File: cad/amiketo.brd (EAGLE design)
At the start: 64 x 35 mm, 58 parts, among them CN1 MICROSDPLAIN, J1 HEADER-5X1, Q1 IRLML6344TRPBF, Q2 DMP2035U-7, SW2 SWITCHKMR211, SW3 SWITCHKMR211, U1 STM32F411/48, U2 LSM303D, U3 ADP5062, U4 MCP1824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

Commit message: lis3dh accel
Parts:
- removed C12: 4.7u, jaw:SMD0603
- removed C13: .22u, jaw:SMD0603
- U2: value LSM303D -> LIS3DH
- moved C14 8.00 mm to (34.5, 31.0)
- moved U2 1.12 mm to (38.0, 31.0)
- moved D1 0.54 mm to (32.5, 31.0)
- moved NOISY1 0.50 mm to (27.7, 31.3)
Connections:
- removed net N$1: C12.1, U2.15
- removed net N$2: C13.2, U2.3
- removed net N$4: C13.1, U2.2
- net GND: no longer C12.2, U2.13, U2.16
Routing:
- net N$4: track 7.66 -> 0.00 mm
- net N$2: track 5.94 -> 0.00 mm
- net GND: track 146.6 -> 141.6 mm, vias 79 -> 80
- net IMUINT: track 22.5 -> 18.7 mm
- net I2CCL: track 111.4 -> 108.8 mm, vias 3 -> 4
- net VCC: track 67.7 -> 70.1 mm, vias 15 -> 13
- net N$1: track 2.31 -> 0.00 mm
- net I2CDA: track 110.5 -> 109.9 mm, vias 5 -> 4
- net N$14: track 11.5 -> 10.9 mm

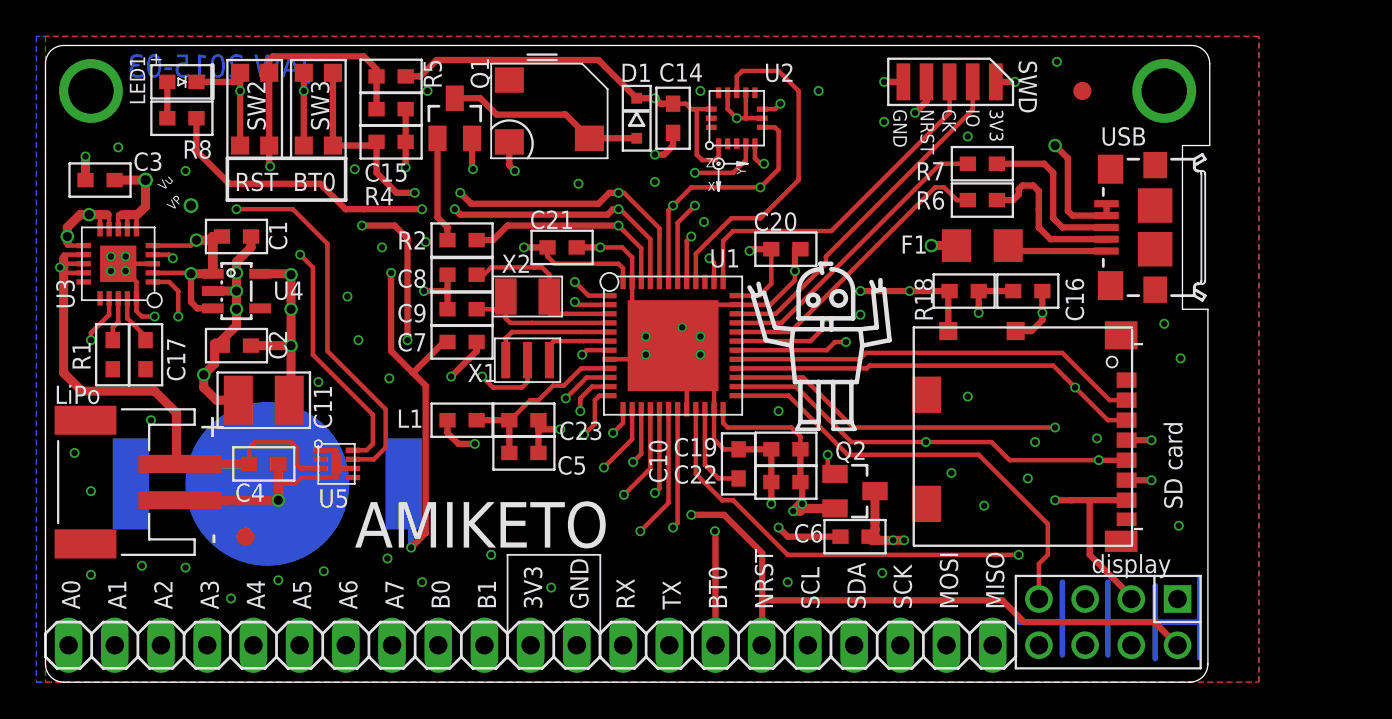
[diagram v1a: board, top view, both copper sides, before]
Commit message: move usb, embiggen sd
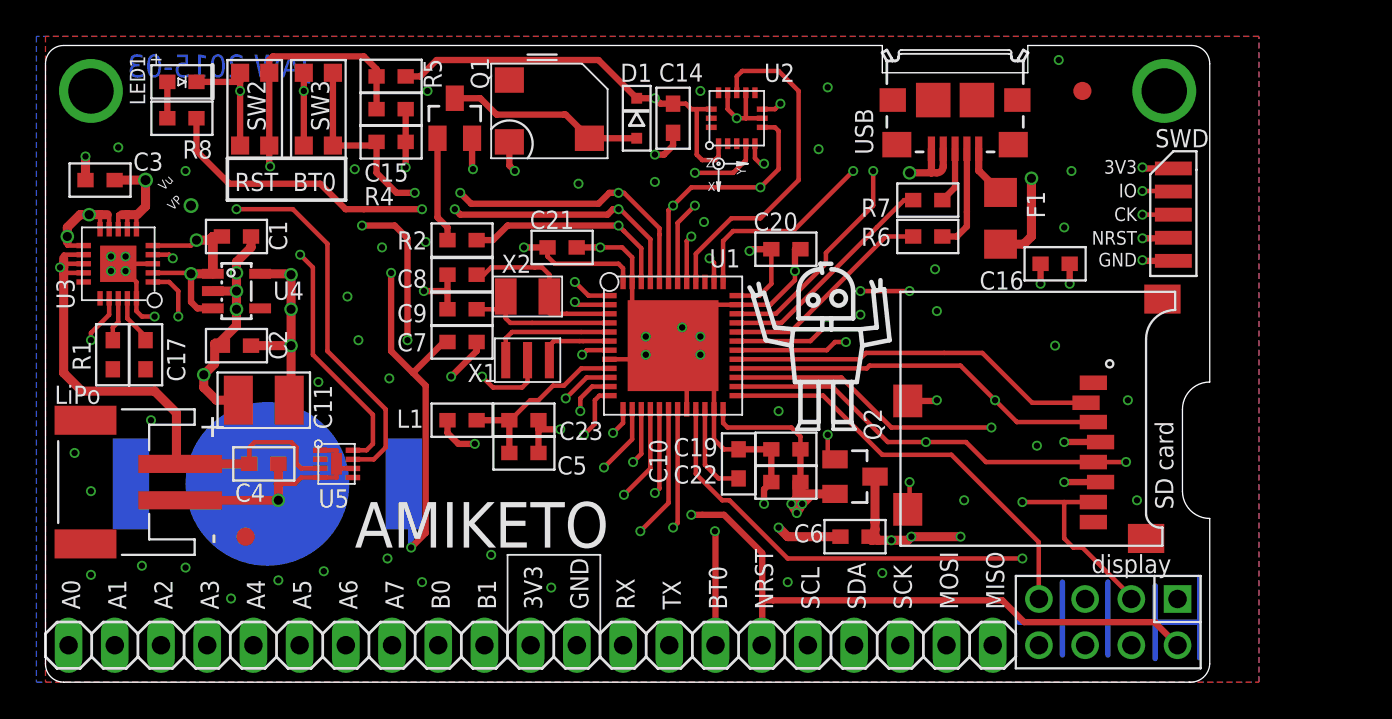
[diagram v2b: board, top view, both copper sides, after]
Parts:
- removed R18: 100k, jaw:SMD0603
- CN1: value MICROSDPLAIN -> MICROSD-EJECT; device jaw:MICROSD/MOLEX/FRONT/PLAIN -> jaw:MICROSD/EJECTOR
- moved J1 14.3 mm to (62.0, 25.7), turned to 270 degrees
- moved USB1 13.0 mm to (50.0, 32.0), turned to 180 degrees
- moved R6 3.61 mm to (48.5, 24.5)
- moved R7 3.61 mm to (48.5, 26.5)
- moved C16 2.12 mm to (55.5, 23.0)
- moved F1 1.80 mm to (52.5, 25.5), turned to 270 degrees
- moved CN1 1.12 mm to (54.5, 14.5)
- moved Q2 0.80 mm to (44.5, 11.3)
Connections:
- net GND: now also CN1.SHELL1; no longer R18.2
- net IOCARD: now also CN1.CD1; no longer CN1.SW2, R18.1
- net VCCE: no longer CN1.SW1
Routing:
- net NRST: track 128.7 -> 111.9 mm
- net VUSB: track 84.3 -> 70.7 mm
- net SWDCK: track 19.3 -> 29.6 mm, vias 0 -> 2
- net SWDIO: track 19.4 -> 29.4 mm, vias 0 -> 2
- net IOCARD: track 17.6 -> 25.2 mm, vias 3 -> 4
- net N$8: track 8.94 -> 3.11 mm
- net USBDM: track 16.3 -> 11.9 mm
- net VCC: track 70.1 -> 74.3 mm, vias 13 -> 14
- net USBDP: track 16.3 -> 12.5 mm
- net SPIMISO: track 43.0 -> 39.5 mm
- net N$7: track 8.93 -> 5.85 mm
- net N$3: track 5.70 -> 2.90 mm
- net VCCE: track 9.50 -> 11.9 mm, vias 4 -> 5
- net SPISCK: track 48.0 -> 45.7 mm
- net SDCS: track 22.6 -> 20.5 mm
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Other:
- outline, holes or cut-outs redrawn

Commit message: 22pin connector
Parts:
- added C12: .1u, jaw:SMD0603
- JP1: value HEADER-21X1 -> HEADER-22X1-PTH; device jaw:HEADER-21X1-PTH -> jaw:HEADER-22X1-PTH
- moved CN6 2.54 mm to (61.0, 3.30)
- moved CN1 2.50 mm to (57.0, 14.5)
- moved J1 2.50 mm to (64.5, 25.7)
- moved U$2 2.50 mm to (59.5, 32.5)
- moved C16 1.50 mm to (57.0, 23.0)
- moved Q2 1.04 mm to (45.5, 11.0)
- moved C6 1.00 mm to (45.5, 8.00)
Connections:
- net BOOT0: now also JP1.16; no longer JP1.15
- net GND: now also C12.2, JP1.13; no longer JP1.12
- net I2CCL: now also JP1.18; no longer JP1.17
- net I2CDA: now also JP1.19; no longer JP1.18
- net NRST: now also JP1.17; no longer JP1.16
- net RX: now also JP1.14; no longer JP1.13
- net SPIMISO: now also JP1.22; no longer JP1.21
- net SPIMOSI: now also JP1.21; no longer JP1.20
- net SPISCK: now also JP1.20; no longer JP1.19
- net TX: now also JP1.15; no longer JP1.14
- net VCC: now also C12.1
- net VUSB: now also JP1.12
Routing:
- net VUSB: track 70.7 -> 114.5 mm
- net VCC: track 74.3 -> 98.2 mm, vias 14 -> 15
- net SPIMISO: track 39.5 -> 42.8 mm
- net DPYCS: track 23.1 -> 26.0 mm
- net SPIMOSI: track 51.3 -> 54.0 mm
- net SPISCK: track 45.7 -> 48.3 mm
- net GND: track 139.8 -> 142.4 mm, vias 80 -> 82
- net DPYDC: track 30.6 -> 33.1 mm
- net SWDIO: track 29.4 -> 31.9 mm
- net SDCS: track 20.5 -> 23.0 mm
- net SWDCK: track 29.6 -> 32.1 mm
- net TX: track 30.1 -> 27.9 mm
- net RX: track 31.8 -> 29.7 mm
- net IOCARD: track 25.2 -> 27.0 mm
- net VCCE: track 11.9 -> 10.2 mm
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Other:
- board size 64 x 35 mm -> 66.5 x 35 mm
- board text added: "VUSB"

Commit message: tweak
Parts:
- moved U2 0.50 mm to (38.5, 31.0)
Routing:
- net VCC: track 98.2 -> 98.7 mm
- net IMUINT: track 18.7 -> 19.2 mm
- net I2CCL: track 107.7 -> 108.2 mm
- net GND: track 142.4 -> 142.1 mm, vias 82 -> 88
- added copper zone on layer 1, net N$1
- added copper zone on layer 1, net N$10
- added copper zone on layer 1, net N$2
- added copper zone on layer 1, net N$4
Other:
- outline, holes or cut-outs redrawn
- board text added: "CR1216/1220"
- board text added: "battery"
- board text added: "bottom layer of 4"
- board text added: "top layer of 4"
- board text added: "|>|"
- board text removed: "JAW 2015-03"
- board text removed: "battery - CR1216"

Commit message: tweak, silk
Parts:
- C6: value 1u -> .1u
- F1: value (none) -> FUSE; device adafruit:R1206 -> jaw:SMD1206
- J1: device jaw:M127-5X1 -> jaw:HEADER-5X1-SMD127-NOCR
- moved C16 0.20 mm to (57.0, 23.2)
- moved U$1 0.10 mm to (43.0, 18.3)
- renumbered NOISY1 to SPKR1
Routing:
- net VUSB: track 114.5 -> 111.1 mm
- net GND: track 142.1 -> 139.4 mm, vias 88 -> 86
- net NPWREN: track 21.7 -> 20.7 mm
- net VCC: track 98.7 -> 99.2 mm
- added copper zone on layer 15, net N$17
- added copper zone on layer 2, net N$19
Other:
- outline, holes or cut-outs redrawn
- board text added: "5 mm"
- board text added: "SD card access KEEP CLEAR!"
- board text added: "inner layer of 4"
- board text added: "use screw: M2.5, No. 3, or 3/32""

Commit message: tweak
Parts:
- added D2: 1A, jaw:SMD0805D
- D1: value DIODESOD-323 -> 200mA
- F1: value FUSE -> 750mA
- USB1: value CON-USB-F-MICRO-B -> (none)
- moved R6 1.00 mm to (48.5, 23.5)
- moved R7 1.00 mm to (48.5, 25.5)
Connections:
- removed net VUSB: C3.1, F1.2, JP1.12, U3.6, U3.7, U3.8
- new net N$24: D2.A, F1.2
- new net VIN: C3.1, D2.C, JP1.12, U3.6, U3.7, U3.8
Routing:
- net VIN: track 0.00 -> 114.9 mm, vias 0 -> 2
- net VUSB: track 111.1 -> 0.00 mm, vias 2 -> 0
- net N$24: track 0.00 -> 5.98 mm
- net IOA3: track 33.2 -> 31.8 mm
- net IOA2: track 37.2 -> 36.1 mm
- net N$8: track 3.11 -> 4.11 mm
- net N$7: track 5.85 -> 6.85 mm
- net IOA1: track 38.9 -> 38.3 mm
- net IOA5: track 28.3 -> 27.7 mm
- added copper zone on layer 16, net N$25
- added copper zone on layer 1, net N$26
- added copper zone on layer 1, net N$27
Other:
- board text added: "VIN"
- board text removed: "+"
- board text removed: "VUSB"
- board text removed: "Vu"
- board text removed: "|>|"

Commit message: i2c r, tweak
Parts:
- added R3, R9: 10k, jaw:SMD0603
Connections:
- net I2CCL: now also R3.1
- net I2CDA: now also R9.1
- net VCC: now also R3.2, R9.2
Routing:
- net VCC: track 99.4 -> 102.4 mm
- net I2CDA: track 109.2 -> 110.5 mm
- net BOOT0: track 63.8 -> 62.5 mm
- net I2CCL: track 108.2 -> 109.1 mm
- net IOB8: track 31.4 -> 31.1 mm, vias 3 -> 2
- net IOB9: vias 1 -> 0
- net GND: vias 86 -> 87
- added copper zone on layer 1, net N$28
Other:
- board text added: "3"

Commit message: swap regulator
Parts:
- removed CN6: (no value), jaw:HEADER-2X04
- removed U4: MCP1824, jaw:SOT-23-5
- added CONN1: HEADER-5X2-PTH, jaw:HEADER-5X2-PTH
- added R10, R11: 1M, jaw:SMD0603
- added VR1: mcp1700 /3v3, jaw:SOT-23-3
- moved U$1 5.39 mm to (48.3, 17.3)
- moved U$4 3.01 mm to (59.0, 23.3)
- moved LOGO1 2.62 mm to (42.0, 22.0)
- moved CN1 2.50 mm to (59.5, 14.5)
- moved J1 2.50 mm to (67.0, 25.7)
- moved U$2 2.50 mm to (62.0, 32.5)
- moved Q1 1.53 mm to (22.8, 32.5)
- moved C6 1.00 mm to (44.5, 8.00)
- moved C12 0.51 mm to (57.5, 25.1)
- moved C1 0.50 mm to (10.5, 25.0), turned to 180 degrees
- moved C16 0.50 mm to (57.5, 23.2)
- moved D2 0.50 mm to (57.5, 27.0)
- moved SPKR1 0.30 mm to (28.0, 31.3)
- moved R9 0.20 mm to (14.0, 23.5)
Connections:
- net DPYCS: now also CONN1.7; no longer CN6.7
- net DPYDC: now also CONN1.6; no longer CN6.6
- net GND: now also CONN1.8, R10.2, VR1.1; no longer CN6.8, U4.2
- net I2CCL: now also CONN1.9
- net I2CDA: now also CONN1.10
- net N$9: now also R10.1
- net NPWREN: now also R11.2
- net NRST: now also CONN1.2; no longer CN6.2
- net SPIMISO: now also CONN1.3; no longer CN6.3
- net SPIMOSI: now also CONN1.5; no longer CN6.5
- net SPISCK: now also CONN1.4; no longer CN6.4
- net VCC: now also R11.1, VR1.2; no longer U4.5
- net VCCE: now also CONN1.1; no longer CN6.1
- net VP: now also VR1.3; no longer U4.1, U4.3
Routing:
- net I2CCL: track 109.1 -> 124.1 mm
- net I2CDA: track 110.5 -> 123.1 mm
- net GND: track 138.9 -> 145.4 mm, vias 87 -> 86
- net VCC: track 102.4 -> 96.8 mm, vias 15 -> 16
- net SPIMISO: track 42.8 -> 48.0 mm
- net NRST: track 113.3 -> 118.4 mm
- net SPIMOSI: track 54.0 -> 57.9 mm
- net VP: track 22.8 -> 19.2 mm
- net SPISCK: track 48.3 -> 51.3 mm
- net SWDCK: track 32.1 -> 34.6 mm
- net SDCS: track 23.0 -> 25.5 mm
- net SWDIO: track 31.9 -> 34.4 mm
- net DPYCS: track 26.0 -> 28.5 mm
- net DPYDC: track 33.1 -> 35.6 mm
- net NPWREN: track 20.7 -> 23.2 mm
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- removed copper zone on layer 15, net N$17
- removed copper zone on layer 2, net N$19
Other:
- board size 66.5 x 35 mm -> 69 x 35 mm
- board text removed: "VP"
- board text removed: "inner layer of 4"
